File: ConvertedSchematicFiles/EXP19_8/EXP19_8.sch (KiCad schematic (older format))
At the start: 11 parts

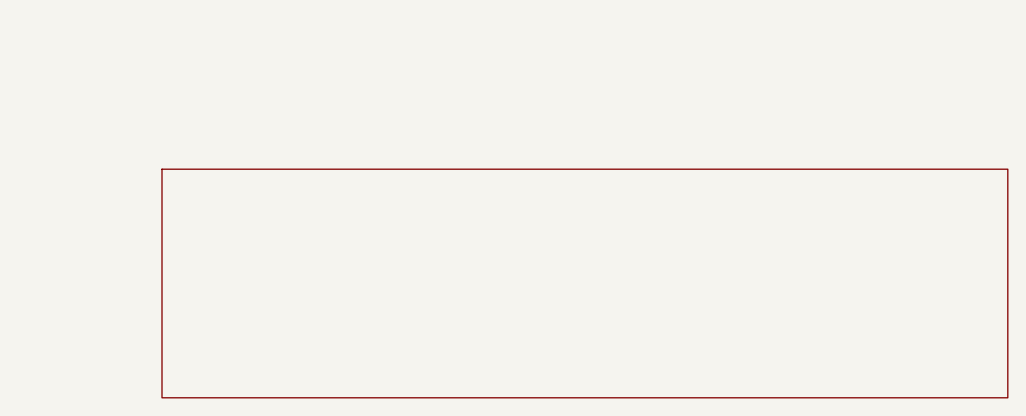
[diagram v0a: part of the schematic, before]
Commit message: Excluded some components. These no longer appear after conversion. When calling shell commands, filenames are in "quotes"
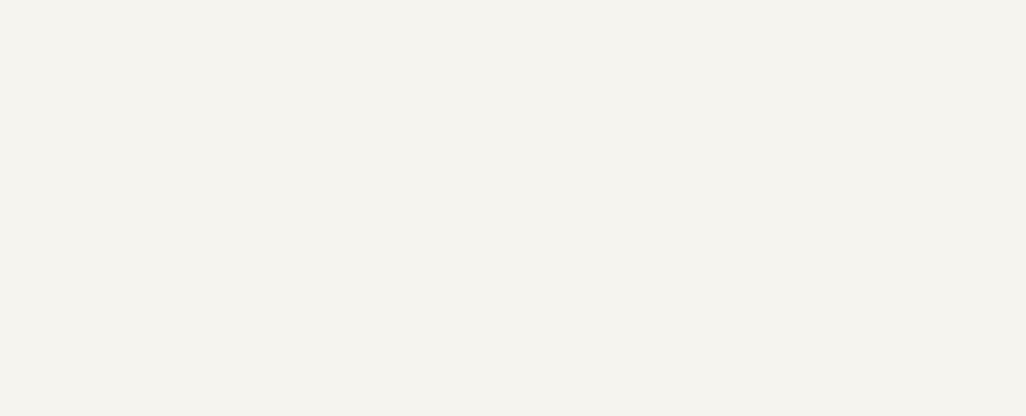
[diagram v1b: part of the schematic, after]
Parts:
- removed titleblk: titleblk, symbol TITLEBLK_PSPICE
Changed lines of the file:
@@
 	0    -1    1    0
-$EndComp
-$Comp
-L TITLEBLK_PSPICE titleblk
-U 1 1 45202362
-P 9700 7200
-F 0 "titleblk" H 19400 14400 30  0001 L CNN
-F 1 "titleblk" H 19400 14480 30  0001 L CNN
-	1    9700 7200
-	1    0    0    1
 $EndComp
 Wire Wire Line

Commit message: Ports issue fixed. Now annotation for ports is #PWR? function added "itos"
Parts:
- removed EGND (x5): EGND, symbol EGND_PSPICE
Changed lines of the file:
@@
 $EndDescr
 $Comp
-L EGND_PSPICE EGND
+L EGND_PSPICE #PWR1
 U 1 1 14289383
 P 1700 3100
-F 0 "EGND" H 3400 6200 30  0001 L CNN
+F 0 "#PWR1" H 3400 6200 30  0001 L CNN
 F 1 "EGND" H 3400 6280 30  0001 L CNN
 	1    1700 3100
@@
 $EndComp
 $Comp
-L EGND_PSPICE EGND
+L EGND_PSPICE #PWR2
 U 1 1 46930886
 P 1000 3000
-F 0 "EGND" H 2000 6000 30  0001 L CNN
+F 0 "#PWR2" H 2000 6000 30  0001 L CNN
 F 1 "EGND" H 2000 6080 30  0001 L CNN
 	1    1000 3000
@@
 $EndComp
 $Comp
-L EGND_PSPICE EGND
+L EGND_PSPICE #PWR3
 U 1 1 71692777
 P 1400 3000
-F 0 "EGND" H 2800 6000 30  0001 L CNN
+F 0 "#PWR3" H 2800 6000 30  0001 L CNN
 F 1 "EGND" H 2800 6080 30  0001 L CNN
 	1    1400 3000
@@
 $EndComp
 $Comp
-L EGND_PSPICE EGND
+L EGND_PSPICE #PWR4
 U 1 1 14636915
 P 700 3300
-F 0 "EGND" H 1400 6600 30  0001 L CNN
+F 0 "#PWR4" H 1400 6600 30  0001 L CNN
 F 1 "EGND" H 1400 6680 30  0001 L CNN
 	1    700 3300
@@
 $EndComp
 $Comp
-L EGND_PSPICE EGND
+L EGND_PSPICE #PWR5
 U 1 1 77747793
 P 2300 2400
-F 0 "EGND" H 4600 4800 30  0001 L CNN
+F 0 "#PWR5" H 4600 4800 30  0001 L CNN
 F 1 "EGND" H 4600 4880 30  0001 L CNN
 	1    2300 2400

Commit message: Added LICENSE.txt
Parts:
- V2: value VPULSE -> PULSE
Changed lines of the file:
@@
 $EndDescr
 $Comp
-L EGND_PSPICE #PWR1
+L GND #PWR1
 U 1 1 14289383
 P 1700 3100
@@
 $EndComp
 $Comp
-L EGND_PSPICE #PWR2
+L GND #PWR2
 U 1 1 46930886
 P 1000 3000
@@
 $EndComp
 $Comp
-L EGND_PSPICE #PWR3
+L GND #PWR3
 U 1 1 71692777
 P 1400 3000
@@
 $EndComp
 $Comp
-L EGND_PSPICE #PWR4
+L GND #PWR4
 U 1 1 14636915
 P 700 3300
@@
 $EndComp
 $Comp
-L EGND_PSPICE #PWR5
+L GND #PWR5
 U 1 1 77747793
 P 2300 2400
@@
 P 700 2900
 F 0 "V2" H 700 2900 30  0000 L CNN
-F 1 "VPULSE" H 700 2980 30  0000 L CNN
+F 1 "PULSE" H 700 2980 30  0000 L CNN
 	1    700 2900
 	1    0    0    1

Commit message: Orientation fix. Library components are now inverted, with +ve y axis going up. In Schematic files, +ve y axis is downwards. This is how the KiCad libraries are. As a result of the above fixed, the converted GND is now oriented correctly.
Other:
- moved on the sheet: S1, V1, V2
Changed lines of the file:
@@
 F 1 "EGND" H 3400 6280 30  0001 L CNN
 	1    1700 3100
-	1    0    0    1
+	1    0    0    -1
 $EndComp
 $Comp
@@
 F 1 "EGND" H 2000 6080 30  0001 L CNN
 	1    1000 3000
-	1    0    0    1
+	1    0    0    -1
 $EndComp
 $Comp
@@
 F 1 "EGND" H 2800 6080 30  0001 L CNN
 	1    1400 3000
-	1    0    0    1
+	1    0    0    -1
 $EndComp
 $Comp
@@
 F 1 "EGND" H 1400 6680 30  0001 L CNN
 	1    700 3300
-	1    0    0    1
+	1    0    0    -1
 $EndComp
 $Comp
@@
 F 1 "EGND" H 4600 4880 30  0001 L CNN
 	1    2300 2400
-	1    0    0    1
+	1    0    0    -1
 $EndComp
 $Comp
@@
 F 1 "Sbreak" H 1000 2980 30  0000 L CNN
 	1    1000 2900
-	1    0    0    1
+	1    0    0    -1
 $EndComp
 $Comp
@@
 F 1 "PULSE" H 700 2980 30  0000 L CNN
 	1    700 2900
-	1    0    0    1
+	1    0    0    -1
 $EndComp
 $Comp
@@
 F 1 "10V" H 2300 1890 30  0000 C CNN
 	1    2300 2000
-	1    0    0    1
+	1    0    0    -1
 $EndComp
 $Comp
@@
 F 1 "R" H 1700 2280 30  0000 L CNN
 	1    1700 2200
-	0    -1    1    0
+	0    1    1    0
 $EndComp
 $Comp
@@
 F 1 "0.1u" H 1700 3110 30  0000 L CNN
 	1    1700 2800
-	0    -1    1    0
+	0    1    1    0
 $EndComp
 Wire Wire Line

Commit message: Removed the use of exec, wrote basename function, made integration with eSim easier.
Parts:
- added titleblk: titleblk, symbol titleblk_PSPICE
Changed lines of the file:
@@
-EESchema Schematic File Version 2  date Monday 07 June 1999 11:59:06 PM IST
+EESchema Schematic File Version 2  date
 LIBS:power
 LIBS:device
@@
 LIBS:contrib
 LIBS:valves
-LIBS:ConvertedSchematicFiles/EXP19_8-cache
 EELAYER 25  0
 EELAYER END
@@
 Sheet 1 1
 Title ""
-Date "07 Jun 1999"
+Date ""
 Rev ""
 Comp ""
@@
 	0    1    1    0
 $EndComp
+$Comp
+L titleblk_PSPICE titleblk
+U 1 1 45202362
+P 9700 7200
+F 0 "titleblk" H 19400 14400 30  0001 L CNN
+F 1 "titleblk" H 19400 14480 30  0001 L CNN
+	1    9700 7200
+	1    0    0    -1
+$EndComp
 Wire Wire Line
